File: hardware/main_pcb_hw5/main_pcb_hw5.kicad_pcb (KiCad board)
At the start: 2 copper layers, 100 x 100 mm, 31 parts, among them J1 MEGA BOTTOM, J10 GBA_Slot, J3 CART SLOT TOP ROW, J4 CART SLOT FRONT ROW, J6 5V USB, J7 Conn_01x07, J8 EXP2, J9 EXP1, M2_1 Screw_Terminal_01x01, M2_2 Screw_Terminal_01x01, M2_3 Screw_Terminal_01x01, M2_4 Screw_Terminal_01x01, M2_5 Screw_Terminal_01x01, M2_6 Screw_Terminal_01x01, M2_7 Screw_Terminal_01x01, M2_8 Screw_Terminal_01x01, M2_9 Screw_Terminal_01x01, SW1 VOLTAGE, SW2 POWER, U1 TPS2113PW, U2 DS3231MZ

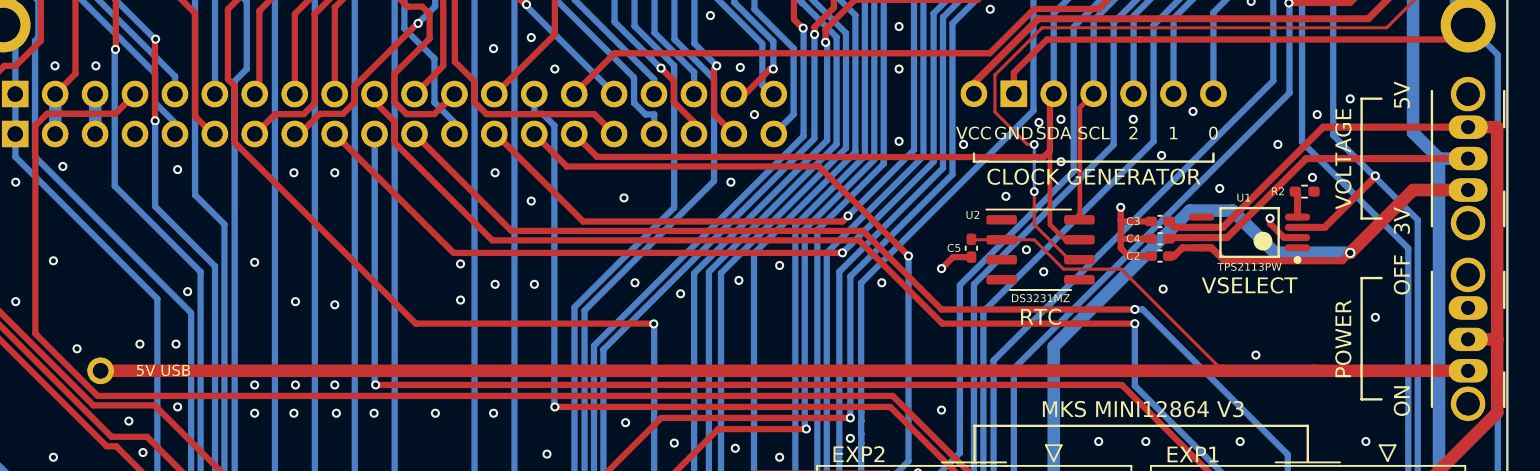
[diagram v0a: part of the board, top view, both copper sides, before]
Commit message: -small mod to routing to no split planes -replace gerber zip -replace pcb renders
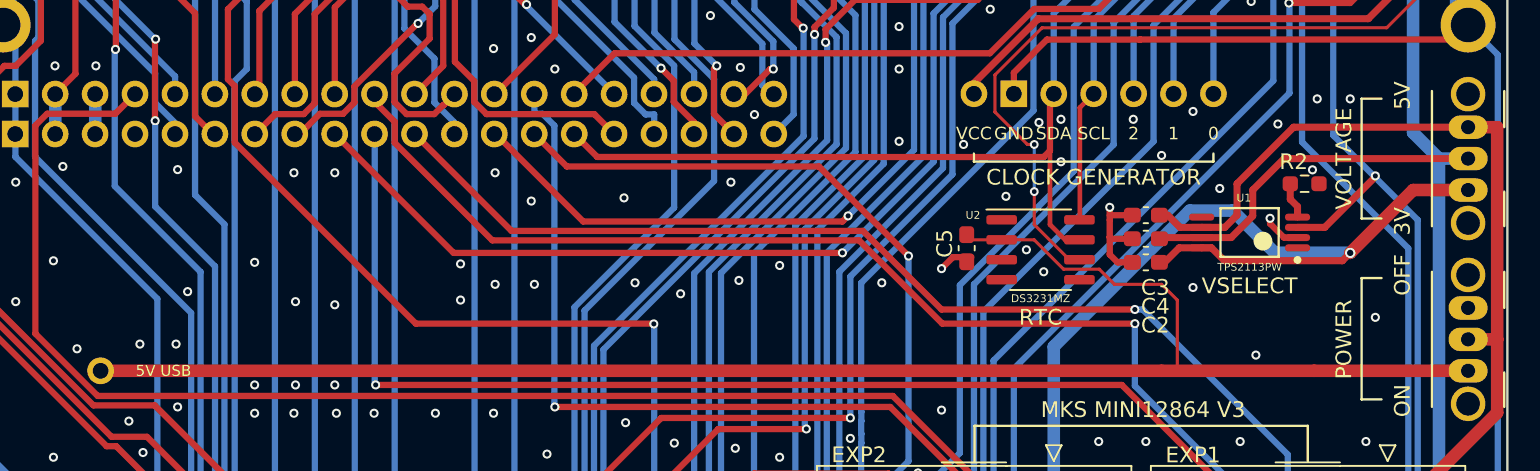
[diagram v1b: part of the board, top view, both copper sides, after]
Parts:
- C2, C3, C4, C5: footprint Capacitor_SMD:C_0402_1005Metric_Pad0.74x0.62mm_HandSolder -> Capacitor_SMD:C_0603_1608Metric_Pad1.08x0.95mm_HandSolder
- R2: footprint Resistor_SMD:R_0402_1005Metric_Pad0.72x0.64mm_HandSolder -> Resistor_SMD:R_0603_1608Metric_Pad0.98x0.95mm_HandSolder
- moved C3 0.98 mm to (177.0, 119.6)
- moved C2 0.98 mm to (177.0, 122.6)
- moved C4 0.90 mm to (177.0, 121.1)
- moved R2 0.50 mm to (187.1, 117.6)
- moved C5 0.30 mm to (165.6, 121.7)
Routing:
- net +5V: track 53.5 -> 55.4 mm
- net VCC: track 282.8 -> 284.4 mm
- net GND: track 382.8 -> 381.9 mm
- net +3V3: track 56.0 -> 56.6 mm
- net Net-(U1-ILIM): track 1.69 -> 2.32 mm
